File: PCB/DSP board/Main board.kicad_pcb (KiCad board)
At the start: 4 copper layers, 60 x 100 mm, 195 parts, among them J201 01x06 male SMD, J701 Conn_01x40_Female, J702 Conn_01x06_Female, J801 1140084168, J901 USB_B, U201 STM32H743II, U401 AS4C32M8SA, U501 CS42448, U601 MIC23050, U602 TPS2113A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

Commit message: Routing done Rev 1
Still need to add some testpoints and art
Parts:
- moved C201 1.20 mm to (238.3, 61.5)
- moved C202 1.20 mm to (237.2, 61.5)
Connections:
- D101 pad 4: +3V3 -> +3V3_MCU
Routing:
- net +3V3: track 212.3 -> 407.0 mm, vias 13 -> 23
- net +5V: track 102.0 -> 211.4 mm, vias 5 -> 9
- net +3V3_USB: track 22.5 -> 44.4 mm, vias 2 -> 5
- net GND: track 1256.2 -> 1274.2 mm, vias 406 -> 412
- net +3V3_MCU: track 111.7 -> 120.9 mm
- net FMC_SDNE0: track 5.09 -> 13.0 mm, vias 0 -> 2
- net DAC1_OUT1: track 76.5 -> 83.4 mm
- net Net-(C201-Pad2): track 2.07 -> 3.62 mm
- net Net-(C202-Pad2): track 2.07 -> 3.62 mm
- net Net-(R603-Pad1): track 2.88 -> 4.41 mm
- net Net-(C506-Pad1): track 1.50 -> 2.99 mm
- net Net-(RN801-Pad6): track 0.00 -> 1.45 mm
- net Net-(C611-Pad1): track 0.00 -> 1.36 mm
- net Net-(RN801-Pad3): track 0.00 -> 1.25 mm

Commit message: Added Testpoints
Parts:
- added TP101: TEST, Measurement_Points:Measurement_Point_Round-SMD-Pad_Small, B.Cu at (247.9, 47.9)
- added TP102: TEST, Measurement_Points:Measurement_Point_Round-SMD-Pad_Small, B.Cu at (247.9, 52.4)
- added TP103: TEST, Measurement_Points:Measurement_Point_Round-SMD-Pad_Small, B.Cu at (247.9, 56.9)
- added TP104: TEST, Measurement_Points:Measurement_Point_Round-SMD-Pad_Small, B.Cu at (211.4, 100.6)
- added TP105: TEST, Measurement_Points:Measurement_Point_Round-SMD-Pad_Small, B.Cu at (211.4, 105.1)
- added TP106: TEST, Measurement_Points:Measurement_Point_Round-SMD-Pad_Small, B.Cu at (253.9, 115.8)
- added TP107: TEST, Measurement_Points:Measurement_Point_Round-SMD-Pad_Small, B.Cu at (229.4, 37.9)
- added TP108: TEST, Measurement_Points:Measurement_Point_Round-SMD-Pad_Small, B.Cu at (229.4, 33.4)
- added TP109: TEST, Measurement_Points:Measurement_Point_Round-SMD-Pad_Small, B.Cu at (253.9, 120.3)
- added TP110: TEST, Measurement_Points:Measurement_Point_Round-SMD-Pad_Small, B.Cu at (202.8, 32.9)
- added TP111: TEST, Measurement_Points:Measurement_Point_Round-SMD-Pad_Small, B.Cu at (207.3, 32.9)
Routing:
- net D-: track 29.8 -> 43.6 mm, vias 0 -> 1
- net D+: track 29.8 -> 42.3 mm, vias 0 -> 1
- net NRST: track 40.1 -> 50.8 mm, vias 3 -> 4
- net PROG_CLK: track 50.3 -> 57.2 mm
- net TFT_LED-: track 39.2 -> 46.0 mm
- net PROG_IO: track 50.5 -> 57.1 mm, vias 5 -> 6
- net +5V: track 211.4 -> 215.5 mm, vias 9 -> 10
- net TFT_LED+: track 22.4 -> 26.2 mm, vias 0 -> 1
- net +3V3: track 407.0 -> 409.5 mm
- net I2C1_SDA: track 73.3 -> 74.8 mm
- net I2C1_SCL: track 75.1 -> 76.6 mm
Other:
- rule trace_min: 0.15 -> 0.1524

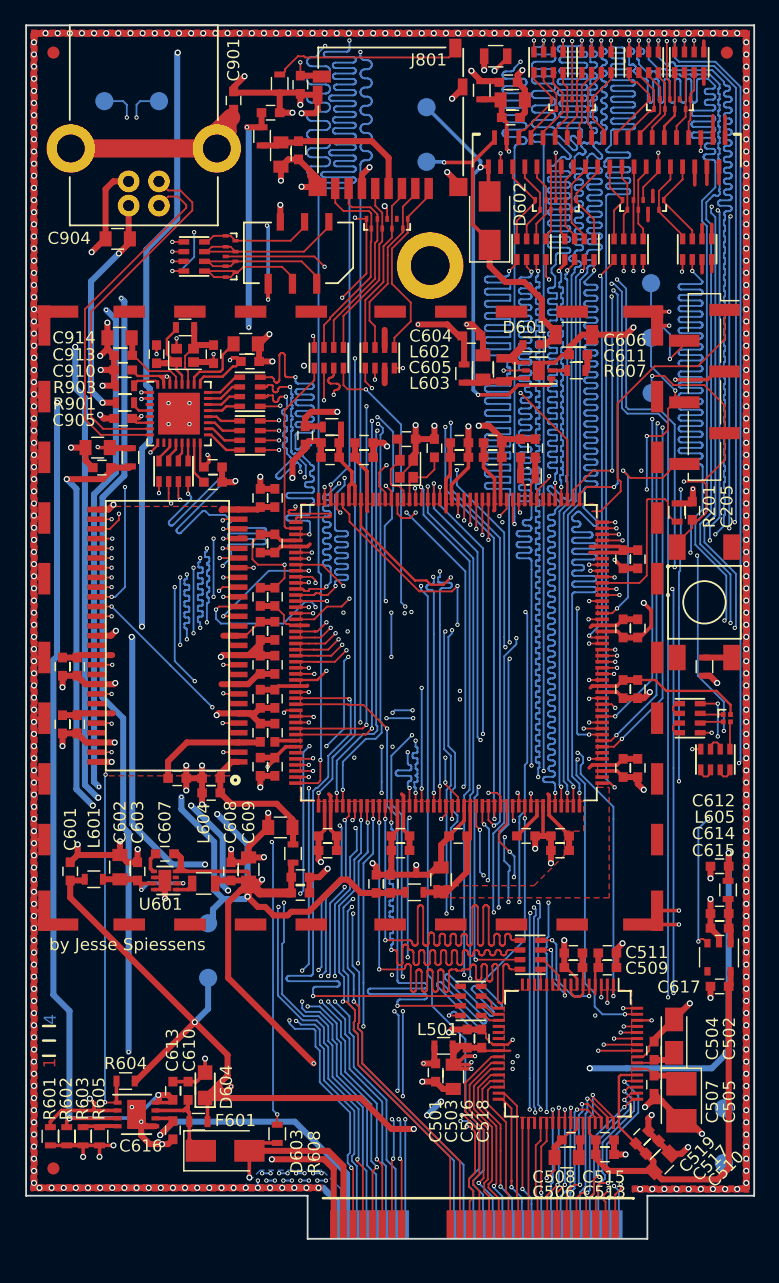
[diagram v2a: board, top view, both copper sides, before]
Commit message: Added ground fills & art
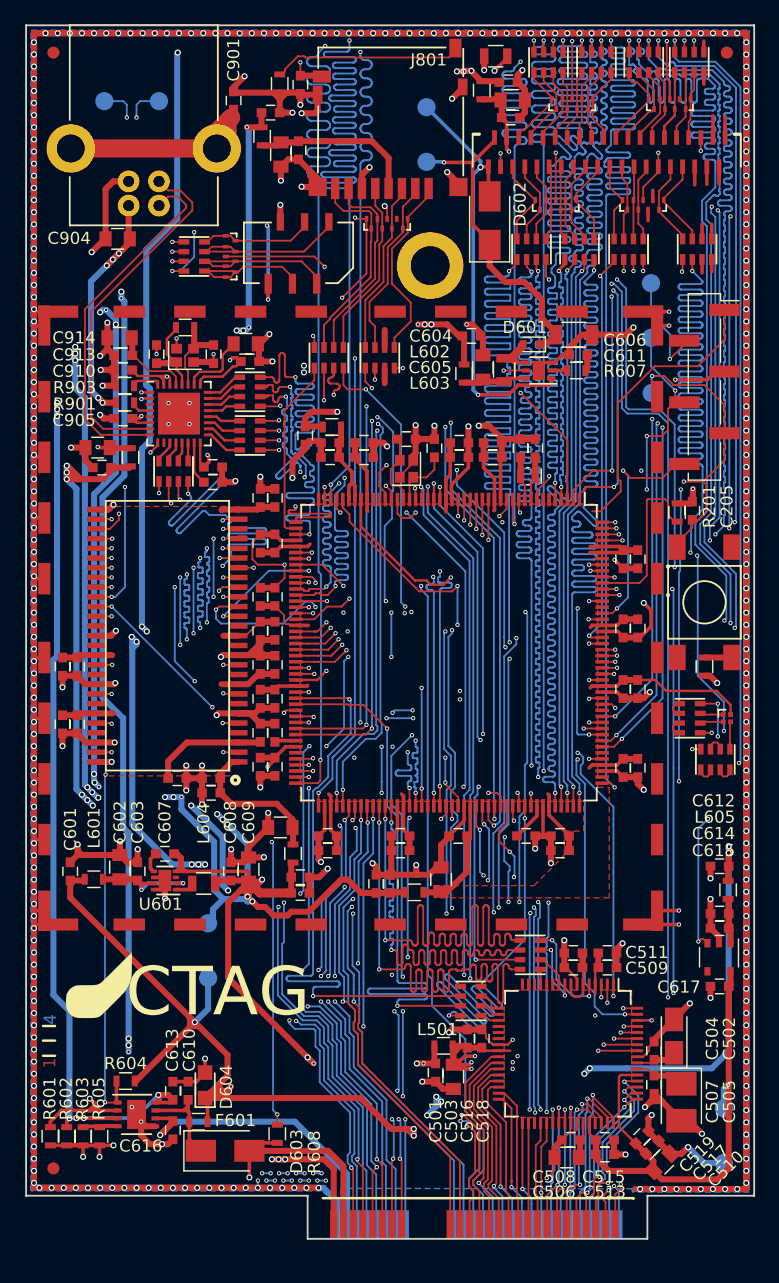
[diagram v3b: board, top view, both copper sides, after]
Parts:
- added G***: LOGO, Graphics:logo_2, B.Cu at (226.5, 60.7)
- added G***: LOGO, CTAG:CTAG, F.Cu at (202.4, 105.7)
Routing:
- net +3V3: track 409.5 -> 442.0 mm, vias 23 -> 51
- net +5V: track 215.5 -> 227.8 mm, vias 10 -> 19
- net VBUS: track 121.2 -> 127.7 mm, vias 6 -> 15
- net GND: track 1274.2 -> 1280.2 mm
- net +3V3_LDO: track 42.0 -> 44.2 mm, vias 0 -> 1
- net Vaux: track 41.2 -> 42.7 mm
- removed copper zone on F.Cu, net GND
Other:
- rule pad_to_mask_clearance: 0.2 -> 0
- board text added: "CTAG"
- board text added: "Cap'n MaGee"
- board text added: "Rev 1.0"
